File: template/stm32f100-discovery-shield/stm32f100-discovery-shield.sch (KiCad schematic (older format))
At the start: 3 parts, among them P1 CONN28, P2 CONN28, P3 CONN6

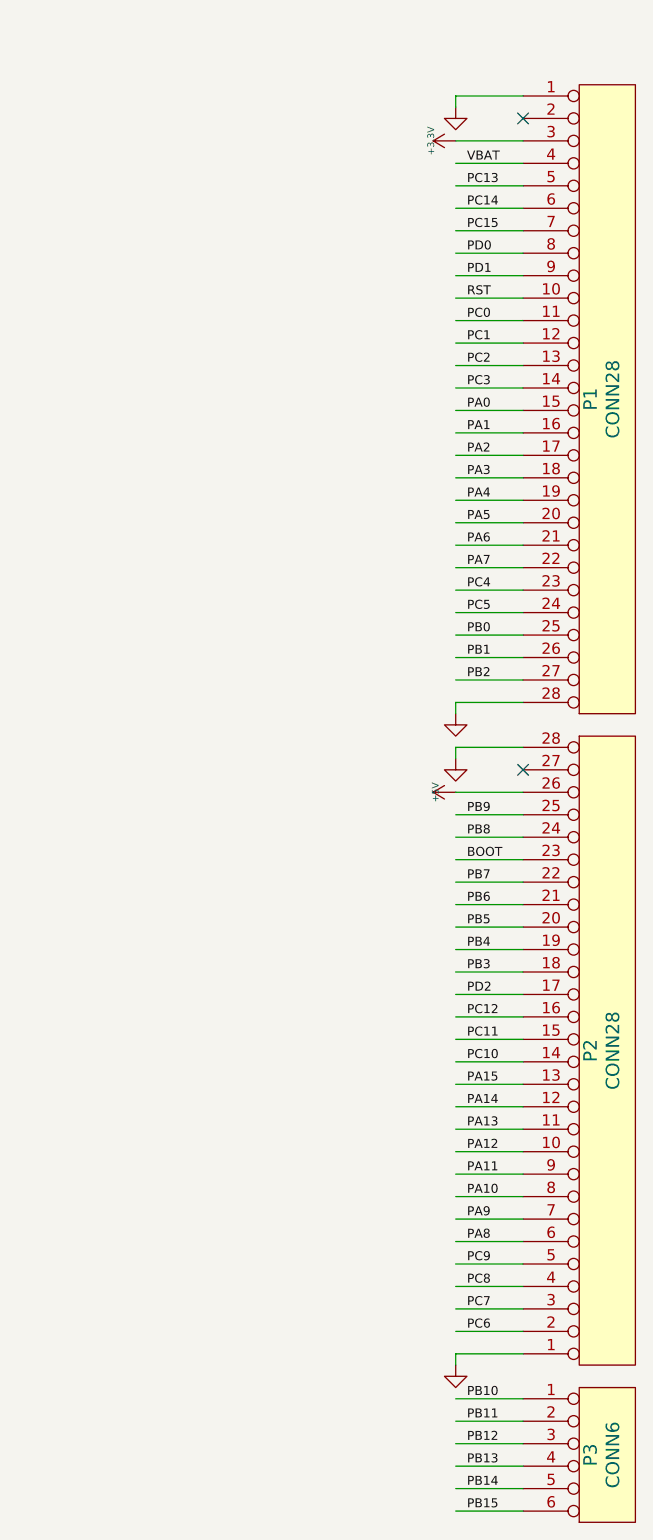
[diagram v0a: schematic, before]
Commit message: fix template
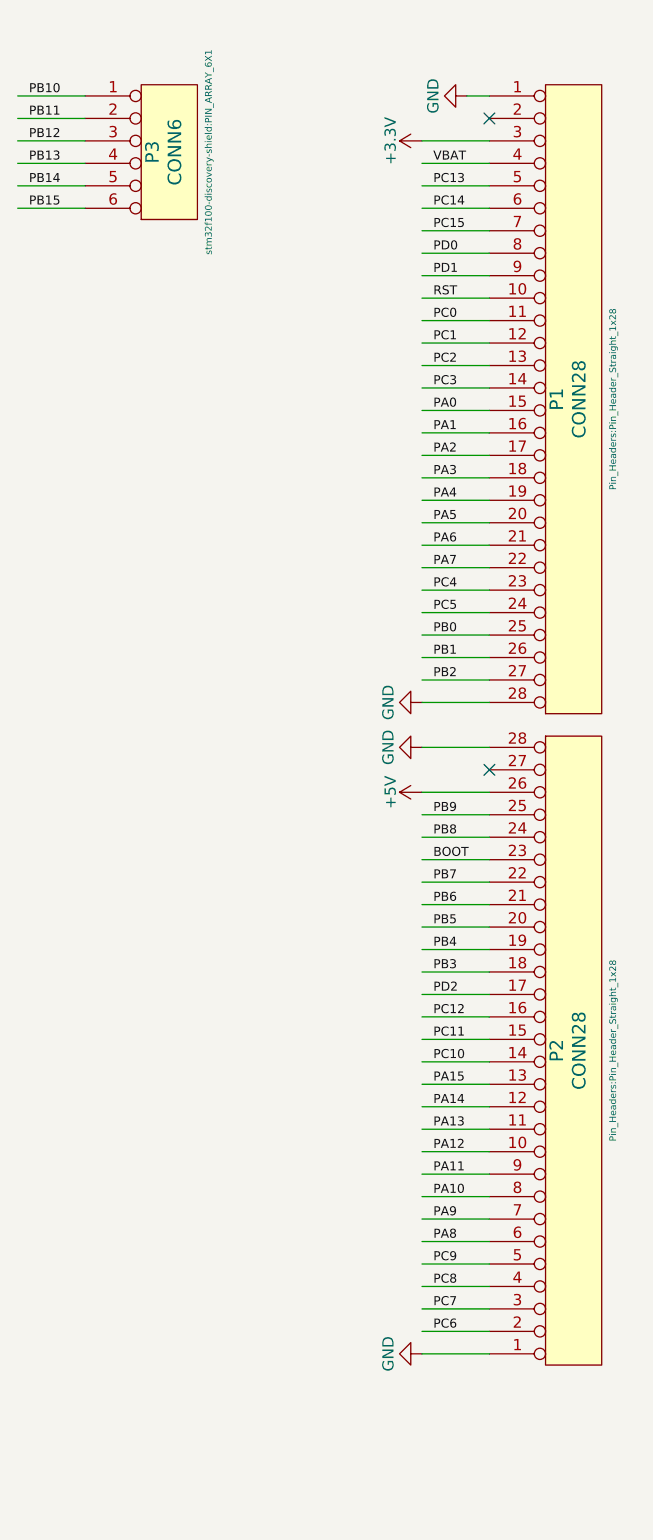
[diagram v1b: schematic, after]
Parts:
- P1, P2: footprint (none) -> Pin_Headers:Pin_Header_Straight_1x28
- P3: footprint (none) -> stm32f100-discovery-shield:PIN_ARRAY_6X1
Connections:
- wire segments 64 -> 60
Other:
- moved on the sheet: P1, P2, P3
